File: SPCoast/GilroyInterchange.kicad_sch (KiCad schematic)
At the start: 40 parts, among them SW5777 777, SW5781 781

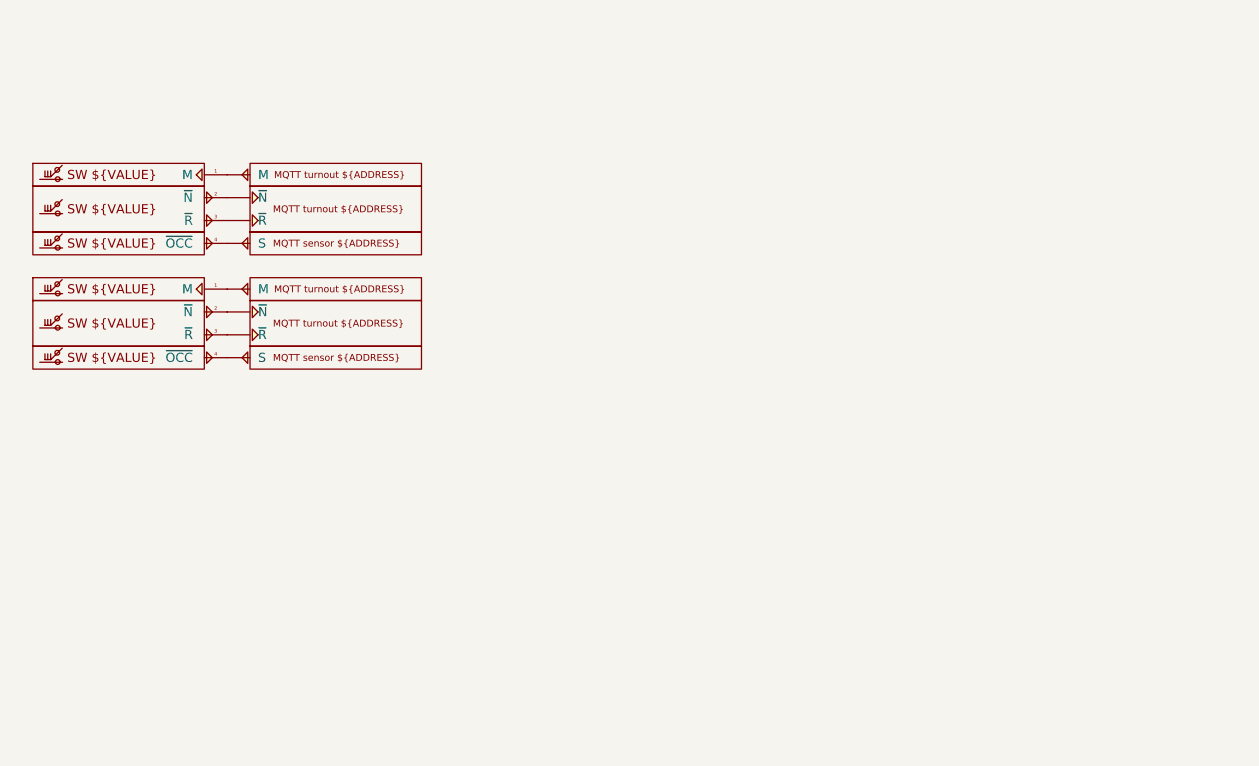
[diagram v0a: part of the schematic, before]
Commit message: chore(kicad): owner edits: GPIO drivers carry Address, Sargent I2C addresses, CMRI body text from fields
Baseline of the owner's saved work before the ADR 0005 scripts:
- Driver-GPIO-Digital and Driver-GPIO-Pixel gain an Address field (the
  board pin); Value renders ${Address}; body text and arrow adjusted.
- Driver-CMRI-IB/OB body text renders UA${Address}.IN/OUT.${Bit} from
  the fields instead of ${VALUE}.
- Sargent, Gilroy Interchange and Luchessa GPIO instances carry Address;
  Sargent Exp2 back at 0x26, Exp3 0x27.
- All sheets resaved by KiCad 10 (reordering), project file
  used_designators cleared by KiCad.

Verified: no lock files; committed as saved, unverified by netlist (the
baseline netlist is exported in the next step).

Co-Authored-By: Claude Fable 5.1 <noreply@anthropic.com>
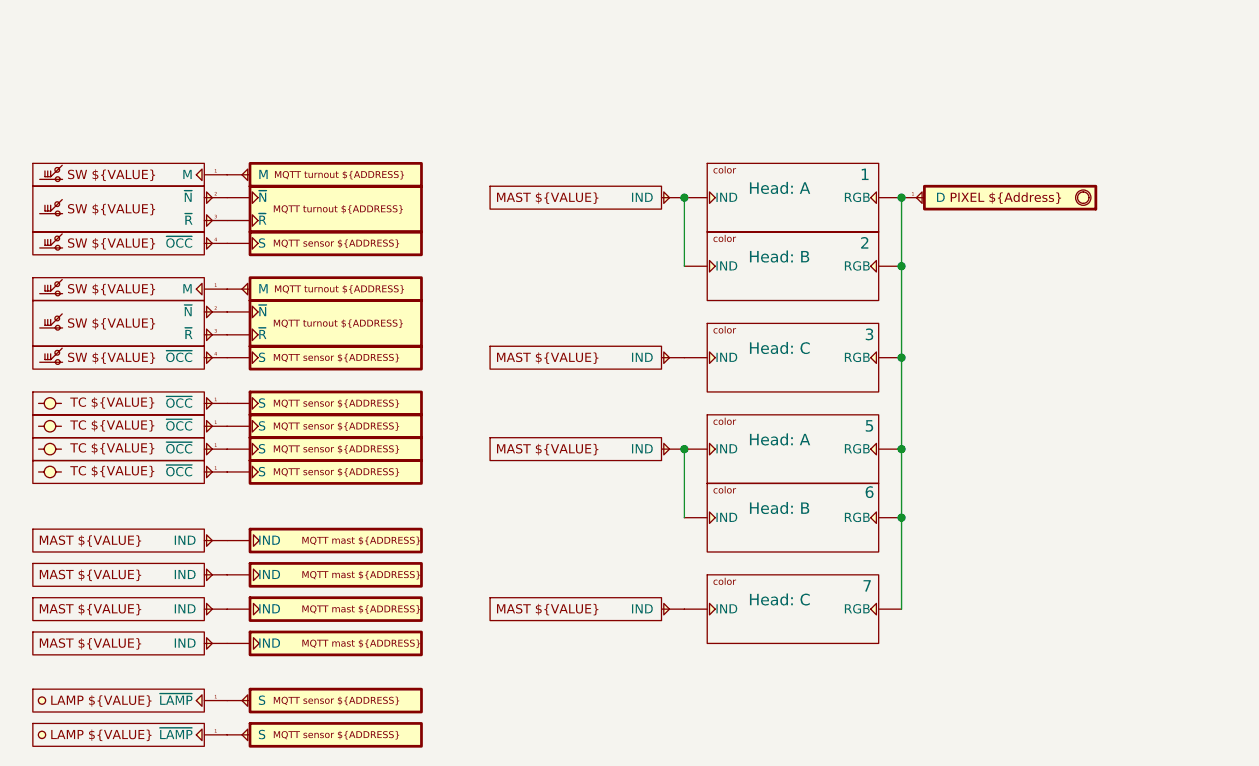
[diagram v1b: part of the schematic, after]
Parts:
- added Cast13, Cast14, Cast15, Cast16, Cast17, Cast18: (no value), symbol Railroad-Field:Cast-Head-Color
- added DevLamp3: MC1, symbol Railroad-Field:Device-Lamp
- added DevLamp4: MC2, symbol Railroad-Field:Device-Lamp
- added DevMast10, DevMast16: 778NC, symbol Railroad-Field:Mast
- added DevMast11, DevMast14: 778SC, symbol Railroad-Field:Mast
- added DevMast12, DevMast15: 778NAB, symbol Railroad-Field:Mast
- added DevMast13, DevMast9: 778SAB, symbol Railroad-Field:Mast
- added DevTC10: 1NAT, symbol Railroad-Field:Device-TrackCircuit-Current
- added DevTC11: 01T, symbol Railroad-Field:Device-TrackCircuit-Current
- added DevTC12: 02T, symbol Railroad-Field:Device-TrackCircuit-Current
- added DevTC9: 1SAT, symbol Railroad-Field:Device-TrackCircuit-Current
- added GPIO5: ${Address}, symbol Railroad-HardwareIO:Driver-GPIO-Pixel
- added JMRI_MQTT10, JMRI_MQTT11, JMRI_MQTT8, JMRI_MQTT9: (no value), symbol Railroad-HardwareIO:Driver-JMRI-Sensor-Feedback
- added JMRI_MQTT12, JMRI_MQTT13, JMRI_MQTT14, JMRI_MQTT7: (no value), symbol Railroad-HardwareIO:Driver-JMRI-SignalMast
- added JMRI_MQTT15, JMRI_MQTT16: (no value), symbol Railroad-HardwareIO:Driver-JMRI-Sensor
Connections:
- new net: DevLamp4.1 (~{LAMP}), JMRI_MQTT16.1 (S)
- new net: Cast13.1 (RGB), Cast14.1 (RGB), Cast15.1 (RGB), Cast16.1 (RGB), Cast17.1 (RGB), Cast18.1 (RGB), GPIO5.1 (D)
- new net: Cast16.2 (IND), Cast17.2 (IND), DevMast15.1 (IND)
- new net: Cast18.2 (IND), DevMast16.1 (IND)
- new net: Cast13.2 (IND), Cast14.2 (IND), DevMast13.1 (IND)
- new net: DevTC10.1 (~{OCC}), JMRI_MQTT9.1 (S)
- new net: DevTC11.1 (~{OCC}), JMRI_MQTT10.1 (S)
- new net: Cast15.2 (IND), DevMast14.1 (IND)
- new net: DevMast10.1 (IND), JMRI_MQTT12.1 (IND)
- new net: DevMast12.1 (IND), JMRI_MQTT14.1 (IND)
- new net: DevTC12.1 (~{OCC}), JMRI_MQTT11.1 (S)
- new net: DevTC9.1 (~{OCC}), JMRI_MQTT8.1 (S)
- new net: DevLamp3.1 (~{LAMP}), JMRI_MQTT15.1 (S)
- new net: DevMast11.1 (IND), JMRI_MQTT13.1 (IND)
- new net: DevMast9.1 (IND), JMRI_MQTT7.1 (IND)
